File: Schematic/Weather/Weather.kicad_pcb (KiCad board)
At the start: 2 copper layers, 38 parts, among them J1 4_Way_Wire, J2 4_Way_Wire, J3 4_Way_Wire, Q1 BSS138, Q2 AO3401, Q3 AO3401, U1 AMS1117, U2 ESP-01v090, U3 AMS1117, U4 ESP-01v090, U5 LM321

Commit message: small compnent changes
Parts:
- moved R1 81.1 mm to (118.1, -120.7), turned to 90 degrees
- moved R2 77.2 mm to (113.0, -120.7), turned to 90 degrees
- moved C3 69.2 mm to (115.6, -116.8), turned to 270 degrees
- moved C2 68.6 mm to (106.7, -114.3), turned to 270 degrees
- moved C1 67.4 mm to (106.7, -128.3), turned to 180 degrees
- moved U2 64.4 mm to (94.0, -123.2), turned to 270 degrees
- moved PSU1 62.0 mm to (160.0, -125.7), turned to 270 degrees
- moved MOD2 60.0 mm to (123.2, -113.0), turned to 90 degrees
- moved J1 57.2 mm to (144.1, -170.0)
- moved U3 57.2 mm to (151.4, -168.2)
- moved U4 57.2 mm to (136.1, -167.9)
- moved U1 54.7 mm to (104.1, -120.7)
- moved R12 51.9 mm to (85.1, -181.6), turned to 270 degrees
- moved Q1 42.6 mm to (24.1, -167.6), turned to 90 degrees
- moved MOD1 41.9 mm to (123.2, -125.7), turned to 90 degrees
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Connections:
- MOD1 pad 2: Net-(MOD1-Pad2) -> GND
- MOD1 pad 3: GND -> /Internal ESP8266/J3_P3
- MOD1 pad 4: /Internal ESP8266/J3_P3 -> /Internal ESP8266/J3_P2
- MOD2 pad 1: /Internal ESP8266/J3_P3 -> /PSU 1/J1_P2
- MOD2 pad 2: /Internal ESP8266/J3_P2 -> GND
- MOD2 pad 3: /PSU 1/J1_P2 -> /Internal ESP8266/J3_P3
- MOD2 pad 4: GND -> /Internal ESP8266/J3_P2
- Q3 pad 2: Net-(Q3-Pad2) -> Vdrive
- R12 pad 1: Net-(R12-Pad1) -> Vdrive

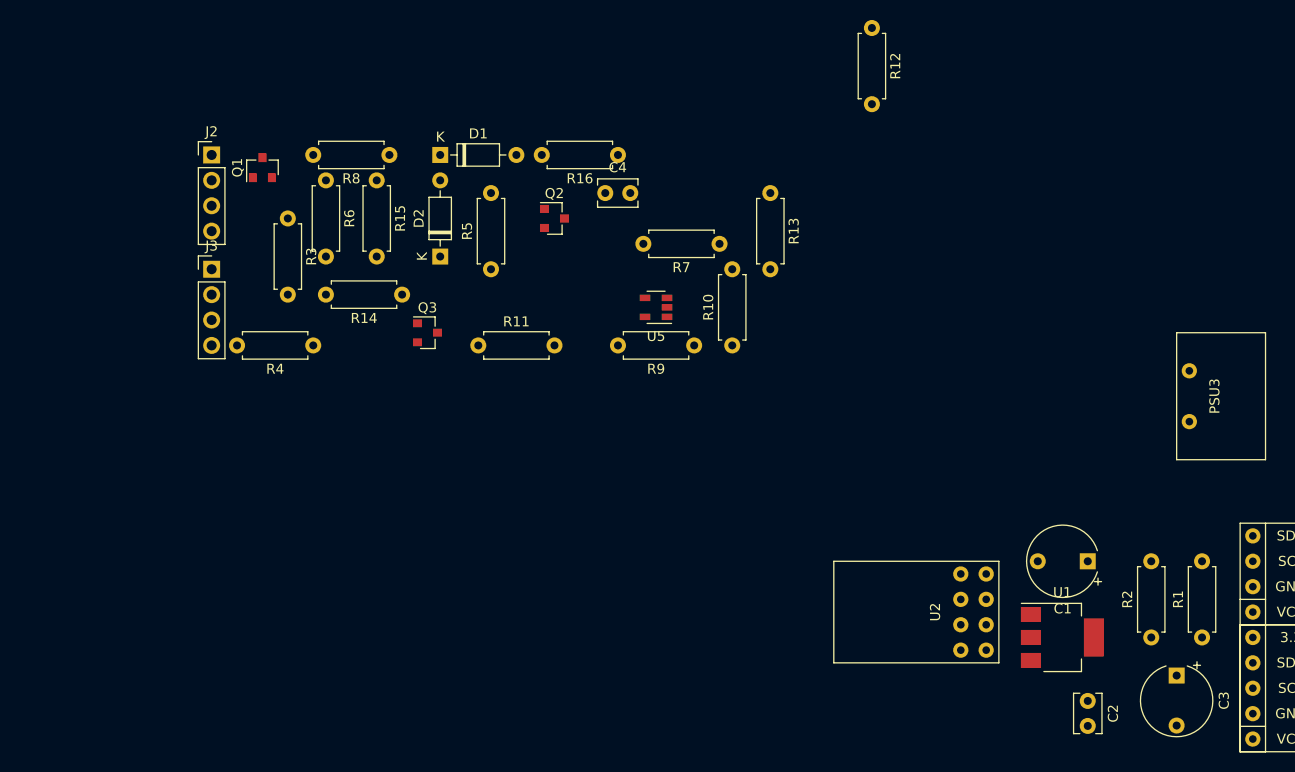
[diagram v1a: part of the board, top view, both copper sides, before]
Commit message: Borad layout 2x for Tx Rx
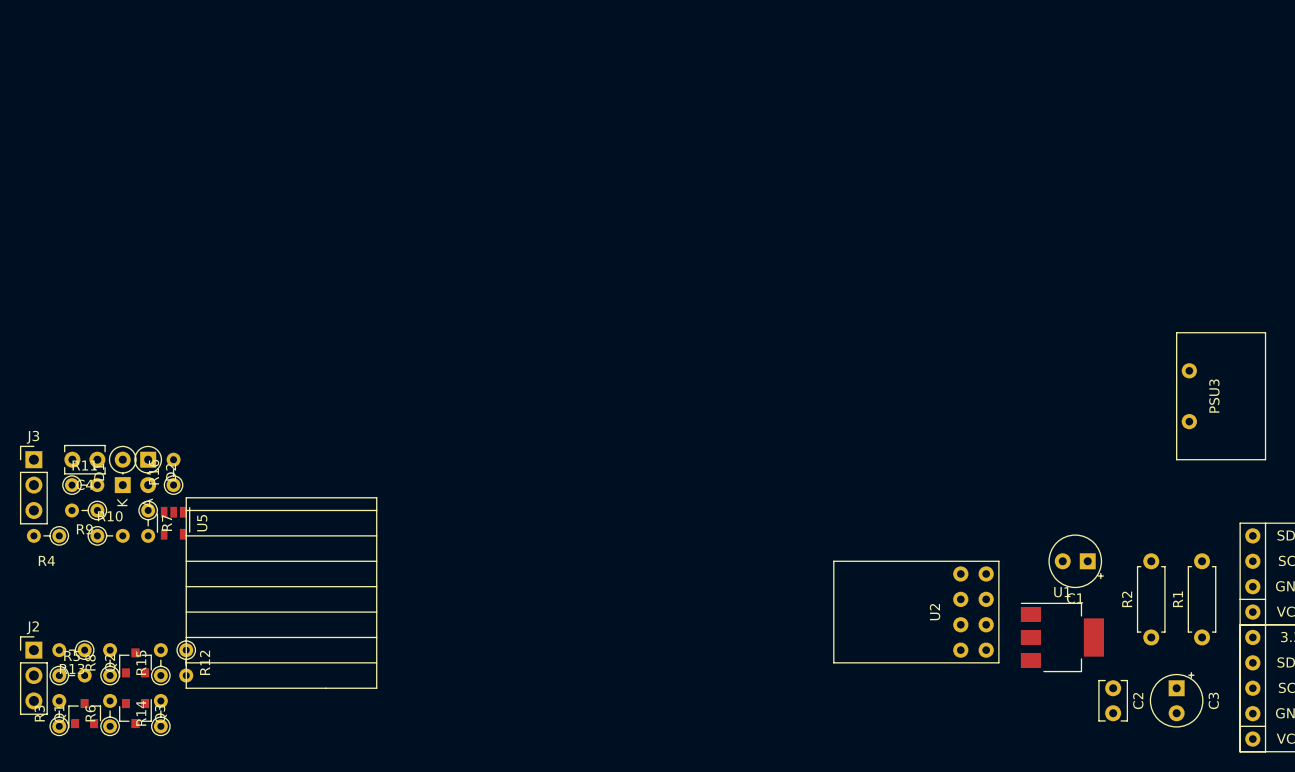
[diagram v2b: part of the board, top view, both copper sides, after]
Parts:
- C1, C3: footprint Capacitor_THT:CP_Radial_Tantal_D7.0mm_P5.00mm -> Capacitor_THT:CP_Radial_Tantal_D5.0mm_P2.50mm
- D1: footprint Diode_THT:D_DO-35_SOD27_P7.62mm_Horizontal -> Diode_THT:D_DO-35_SOD27_P2.54mm_Vertical_KathodeUp
- D2: footprint Diode_THT:D_DO-35_SOD27_P7.62mm_Horizontal -> Diode_THT:D_DO-35_SOD27_P2.54mm_Vertical_AnodeUp
- J2, J3: value 4_Way_Wire -> 3_Way_Wire; footprint Connector_PinHeader_2.54mm:PinHeader_1x04_P2.54mm_Vertical -> Connector_PinHeader_2.54mm:PinHeader_1x03_P2.54mm_Vertical
- R10, R11, R12, R13, R14, R15, R16, R3, R4, R5, R6, R7, R8, R9: footprint Resistor_THT:R_Axial_DIN0207_L6.3mm_D2.5mm_P7.62mm_Horizontal -> Resistor_THT:R_Axial_DIN0204_L3.6mm_D1.6mm_P2.54mm_Vertical
- moved R12 92.6 mm to (16.5, -119.4)
- moved R13 82.4 mm to (6.35, -119.4), turned to 180 degrees
- moved R10 66.3 mm to (7.62, -130.8), turned to 0 degrees
- moved R7 63.1 mm to (12.7, -133.3), turned to 270 degrees
- moved R9 61.9 mm to (7.62, -133.3)
- moved Q2 61.1 mm to (11.4, -118.1), turned to 90 degrees
- moved R5 59.3 mm to (3.81, -116.8), turned to 0 degrees
- moved R8 59.1 mm to (8.89, -116.8), turned to 90 degrees
- moved R6 58.7 mm to (8.89, -111.8), turned to 90 degrees
- moved Q1 57.4 mm to (6.35, -113.0)
- moved C4 57.4 mm to (7.62, -138.4), turned to 180 degrees
- moved R3 55.7 mm to (3.81, -111.8), turned to 90 degrees
- moved R16 55.4 mm to (15.2, -135.9), turned to 90 degrees
- moved R15 54.0 mm to (14.0, -116.8), turned to 90 degrees
- moved U5 52.9 mm to (15.2, -132.1), turned to 270 degrees
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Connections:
- J1 pad 1: Net-(J1-Pad1) -> (no net)
- J1 pad 2: Net-(J1-Pad2) -> (no net)
- J1 pad 3: Net-(J1-Pad3) -> (no net)
- J1 pad 4: Net-(J1-Pad4) -> (no net)
- J2 pad 2: /Anenometer Control Board/J13_P2 -> /Anenometer Control Board/J13_P4
- J2 pad 3: GNDS -> /Anenometer Control Board/J13_P5
- J3 pad 2: /Anenometer Control Board/J13_P6 -> /Anenometer Control Board/J13_P2
- J3 pad 3: GNDS -> /Anenometer Control Board/J13_P3
- PSU2 pad 2: /PSU 2/J5_P2 -> (no net)
- PSU3 pad 2: /PSU 2/J5_P3 -> (no net)
- R3 pad 2: /Anenometer Control Board/J13_P6 -> /Anenometer Control Board/J13_P5
- R4 pad 2: /Anenometer Control Board/J13_P8 -> /Anenometer Control Board/J13_P3
- U2 pad 1: Net-(U2-Pad1) -> (no net)
- U2 pad 8: Net-(U2-Pad8) -> (no net)
- U3 pad 3: Net-(U3-Pad3) -> (no net)
- U4 pad 1: Net-(U4-Pad1) -> (no net)
- U4 pad 3: Net-(U4-Pad3) -> (no net)
- U4 pad 4: Net-(U4-Pad4) -> (no net)
- U4 pad 5: Net-(U4-Pad5) -> (no net)
- U4 pad 6: Net-(U4-Pad6) -> (no net)
- U4 pad 8: Net-(U4-Pad8) -> (no net)

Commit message: board rework
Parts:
- moved R7 2.54 mm to (12.7, -130.8), turned to 90 degrees
- moved U5 1.27 mm to (16.5, -132.1), turned to 0 degrees
- moved J3 1.27 mm to (2.54, -138.4)
- moved R4 1.27 mm to (5.08, -130.8)
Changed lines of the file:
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@@
     (solder_mask_min_width 0.25)
     (aux_axis_origin 0 0)
-    (visible_elements 7FFFEFFF)
+    (visible_elements 7FFFFFFF)
     (pcbplotparams
       (layerselection 0x010fc_ffffffff)
@@
   )
   (module Connector_PinHeader_2.54mm:PinHeader_1x03_P2.54mm_Vertical (layer F.Cu)
-    (at 1.27 -138.43)
+    (at 2.54 -138.43)
     (descr "Through hole straight pin header, 1x03, 2.54mm pitch, single row")
     (tags "Through hole pin header THT 1x03 2.54mm single row")
@@
   )
   (module Resistor_THT:R_Axial_DIN0204_L3.6mm_D1.6mm_P2.54mm_Vertical (layer F.Cu)
-    (at 12.7 -133.35 270)
-    (descr "Resistor, Axial_DIN0204 series, Axial, Vertical, pin pitch=2.54mm, 0.167W, length*diameter=3.6*1.6mm^2, http://cdn-reichelt.de/documents/datenblatt/B400/1_4W%23YAG.pdf")
-    (tags "Resistor Axial_DIN0204 series Axial Vertical pin pitch 2.54mm 0.167W length 3.6mm diameter 1.6mm")
-    (fp_text reference R7 (at 1.27 -1.92 270) (layer F.SilkS)
-      (effects (font (size 1 1) (thickness 0.15)))
-    )
-    (fp_text value 4.7K (at 1.27 1.92 270) (layer F.Fab)
-      (effects (font (size 1 1) (thickness 0.15)))
-    )
-    (fp_text user %R (at 1.27 -1.92 270) (layer F.Fab)
-      (effects (font (size 1 1) (thickness 0.15)))
-    )
-    (fp_line (start 3.49 -1.05) (end -1.05 -1.05) (layer F.CrtYd) (width 0.05))
-    (fp_line (start 3.49 1.05) (end 3.49 -1.05) (layer F.CrtYd) (width 0.05))
-    (fp_line (start -1.05 1.05) (end 3.49 1.05) (layer F.CrtYd) (width 0.05))
-    (fp_line (start -1.05 -1.05) (end -1.05 1.05) (layer F.CrtYd) (width 0.05))
-    (fp_line (start 0.92 0) (end 1.54 0) (layer F.SilkS) (width 0.12))
-    (fp_line (start 0 0) (end 2.54 0) (layer F.Fab) (width 0.1))
-    (fp_circle (center 0 0) (end 0.92 0) (layer F.SilkS) (width 0.12))
-    (fp_circle (center 0 0) (end 0.8 0) (layer F.Fab) (width 0.1))
-    (pad 2 thru_hole oval (at 2.54 0 270) (size 1.4 1.4) (drill 0.7) (layers *.Cu *.Mask)
+    (at 12.7 -130.81 90)
+    (descr "Resistor, Axial_DIN0204 series, Axial, Vertical, pin pitch=2.54mm, 0.167W, length*diameter=3.6*1.6mm^2, http://cdn-reichelt.de/documents/datenblatt/B400/1_4W%23YAG.pdf")
+    (tags "Resistor Axial_DIN0204 series Axial Vertical pin pitch 2.54mm 0.167W length 3.6mm diameter 1.6mm")
+    (fp_text reference R7 (at 1.27 -1.92 90) (layer F.SilkS)
+      (effects (font (size 1 1) (thickness 0.15)))
+    )
+    (fp_text value 4.7K (at 1.27 1.92 90) (layer F.Fab)
+      (effects (font (size 1 1) (thickness 0.15)))
+    )
+    (fp_text user %R (at 1.27 -1.92 90) (layer F.Fab)
+      (effects (font (size 1 1) (thickness 0.15)))
+    )
+    (fp_line (start 3.49 -1.05) (end -1.05 -1.05) (layer F.CrtYd) (width 0.05))
+    (fp_line (start 3.49 1.05) (end 3.49 -1.05) (layer F.CrtYd) (width 0.05))
+    (fp_line (start -1.05 1.05) (end 3.49 1.05) (layer F.CrtYd) (width 0.05))
+    (fp_line (start -1.05 -1.05) (end -1.05 1.05) (layer F.CrtYd) (width 0.05))
+    (fp_line (start 0.92 0) (end 1.54 0) (layer F.SilkS) (width 0.12))
+    (fp_line (start 0 0) (end 2.54 0) (layer F.Fab) (width 0.1))
+    (fp_circle (center 0 0) (end 0.92 0) (layer F.SilkS) (width 0.12))
+    (fp_circle (center 0 0) (end 0.8 0) (layer F.Fab) (width 0.1))
+    (pad 2 thru_hole oval (at 2.54 0 90) (size 1.4 1.4) (drill 0.7) (layers *.Cu *.Mask)
       (net 20 "Net-(R4-Pad1)"))
-    (pad 1 thru_hole circle (at 0 0 270) (size 1.4 1.4) (drill 0.7) (layers *.Cu *.Mask)
+    (pad 1 thru_hole circle (at 0 0 90) (size 1.4 1.4) (drill 0.7) (layers *.Cu *.Mask)
       (net 21 "Net-(R11-Pad2)"))
     (model ${KISYS3DMOD}/Resistor_THT.3dshapes/R_Axial_DIN0204_L3.6mm_D1.6mm_P2.54mm_Vertical.wrl
@@
   )
   (module Resistor_THT:R_Axial_DIN0204_L3.6mm_D1.6mm_P2.54mm_Vertical (layer F.Cu)
-    (at 3.81 -130.81 180)
+    (at 5.08 -130.81 180)
     (descr "Resistor, Axial_DIN0204 series, Axial, Vertical, pin pitch=2.54mm, 0.167W, length*diameter=3.6*1.6mm^2, http://cdn-reichelt.de/documents/datenblatt/B400/1_4W%23YAG.pdf")
     (tags "Resistor Axial_DIN0204 series Axial Vertical pin pitch 2.54mm 0.167W length 3.6mm diameter 1.6mm")
@@
   )
   (module Package_TO_SOT_SMD:SOT-23-5 (layer F.Cu)
-    (at 15.24 -132.08 270)
+    (at 16.51 -132.08)
     (descr "5-pin SOT23 package")
     (tags SOT-23-5)
     (attr smd)
-    (fp_text reference U5 (at 0 -2.9 270) (layer F.SilkS)
-      (effects (font (size 1 1) (thickness 0.15)))
-    )
-    (fp_text value LM321 (at 0 2.9 270) (layer F.Fab)
+    (fp_text reference U5 (at 0 -2.9) (layer F.SilkS)
+      (effects (font (size 1 1) (thickness 0.15)))
+    )
+    (fp_text value LM321 (at 0 2.9) (layer F.Fab)
       (effects (font (size 1 1) (thickness 0.15)))
     )
@@
     (fp_line (start 0.9 -1.61) (end -1.55 -1.61) (layer F.SilkS) (width 0.12))
     (fp_line (start -0.9 1.61) (end 0.9 1.61) (layer F.SilkS) (width 0.12))
-    (fp_text user %R (at 0 0) (layer F.Fab)
+    (fp_text user %R (at 0 0 -270) (layer F.Fab)
       (effects (font (size 0.5 0.5) (thickness 0.075)))
     )
-    (pad 5 smd rect (at 1.1 -0.95 270) (size 1.06 0.65) (layers F.Cu F.Paste F.Mask)
+    (pad 5 smd rect (at 1.1 -0.95) (size 1.06 0.65) (layers F.Cu F.Paste F.Mask)
       (net 8 "/Anenometer Control Board/J13_P2"))
-    (pad 4 smd rect (at 1.1 0.95 270) (size 1.06 0.65) (layers F.Cu F.Paste F.Mask)
+    (pad 4 smd rect (at 1.1 0.95) (size 1.06 0.65) (layers F.Cu F.Paste F.Mask)
       (net 20 "Net-(R4-Pad1)"))
-    (pad 3 smd rect (at -1.1 0.95 270) (size 1.06 0.65) (layers F.Cu F.Paste F.Mask)
+    (pad 3 smd rect (at -1.1 0.95) (size 1.06 0.65) (layers F.Cu F.Paste F.Mask)
       (net 21 "Net-(R11-Pad2)"))
-    (pad 2 smd rect (at -1.1 0 270) (size 1.06 0.65) (layers F.Cu F.Paste F.Mask)
-      (net 6 GNDS))
-    (pad 1 smd rect (at -1.1 -0.95 270) (size 1.06 0.65) (layers F.Cu F.Paste F.Mask)
+    (pad 2 smd rect (at -1.1 0) (size 1.06 0.65) (layers F.Cu F.Paste F.Mask)
+      (net 6 GNDS))
+    (pad 1 smd rect (at -1.1 -0.95) (size 1.06 0.65) (layers F.Cu F.Paste F.Mask)
       (net 22 "Net-(R10-Pad1)"))
     (model ${KISYS3DMOD}/Package_TO_SOT_SMD.3dshapes/SOT-23-5.wrl

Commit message: update before south board added
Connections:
- J1 pad 1: (no net) -> Net-(J1-Pad1)
- J1 pad 2: (no net) -> Net-(J1-Pad2)
- J1 pad 3: (no net) -> Net-(J1-Pad3)
- J1 pad 4: (no net) -> Net-(J1-Pad4)
- PSU2 pad 2: (no net) -> /PSU 2/J5_P2
- PSU3 pad 2: (no net) -> /PSU 2/J5_P3
- U2 pad 1: (no net) -> Net-(U2-Pad1)
- U2 pad 8: (no net) -> Net-(U2-Pad8)
- U3 pad 3: (no net) -> Net-(U3-Pad3)
- U4 pad 1: (no net) -> Net-(U4-Pad1)
- U4 pad 3: (no net) -> Net-(U4-Pad3)
- U4 pad 4: (no net) -> Net-(U4-Pad4)
- U4 pad 5: (no net) -> Net-(U4-Pad5)
- U4 pad 6: (no net) -> Net-(U4-Pad6)
- U4 pad 8: (no net) -> Net-(U4-Pad8)
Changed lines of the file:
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@@
     (zones 0)
     (modules 38)
-    (nets 27)
+    (nets 42)
   )
   (page A4)
@@
     (solder_mask_min_width 0.25)
     (aux_axis_origin 0 0)
-    (visible_elements 7FFFFFFF)
+    (visible_elements 7FFFEFFF)
     (pcbplotparams
       (layerselection 0x010fc_ffffffff)
@@
   (net 25 "/Anenometer Control Board/J13_P5")
   (net 26 "/Anenometer Control Board/J13_P3")
+  (net 27 "Net-(J1-Pad4)")
+  (net 28 "Net-(J1-Pad3)")
+  (net 29 "Net-(J1-Pad2)")
+  (net 30 "Net-(J1-Pad1)")
+  (net 31 "/PSU 2/J5_P2")
+  (net 32 "/PSU 2/J5_P3")
+  (net 33 "Net-(U2-Pad8)")
+  (net 34 "Net-(U2-Pad1)")
+  (net 35 "Net-(U3-Pad3)")
+  (net 36 "Net-(U4-Pad8)")
+  (net 37 "Net-(U4-Pad6)")
+  (net 38 "Net-(U4-Pad5)")
+  (net 39 "Net-(U4-Pad4)")
+  (net 40 "Net-(U4-Pad3)")
+  (net 41 "Net-(U4-Pad1)")
   (net_class Default "This is the default net class."
     (clearance 0.2)
@@
     (add_net "/PSU 1/J1_P2")
     (add_net "/PSU 2/J5_P1")
+    (add_net "/PSU 2/J5_P2")
+    (add_net "/PSU 2/J5_P3")
     (add_net GND)
     (add_net GNDS)
@@
     (add_net "Net-(C4-Pad1)")
     (add_net "Net-(C4-Pad2)")
+    (add_net "Net-(J1-Pad1)")
+    (add_net "Net-(J1-Pad2)")
+    (add_net "Net-(J1-Pad3)")
+    (add_net "Net-(J1-Pad4)")
     (add_net "Net-(Q1-Pad1)")
     (add_net "Net-(Q1-Pad3)")
@@
     (add_net "Net-(R2-Pad2)")
     (add_net "Net-(R4-Pad1)")
+    (add_net "Net-(U2-Pad1)")
+    (add_net "Net-(U2-Pad8)")
     (add_net "Net-(U3-Pad1)")
     (add_net "Net-(U3-Pad2)")
+    (add_net "Net-(U3-Pad3)")
+    (add_net "Net-(U4-Pad1)")
+    (add_net "Net-(U4-Pad3)")
+    (add_net "Net-(U4-Pad4)")
+    (add_net "Net-(U4-Pad5)")
+    (add_net "Net-(U4-Pad6)")
+    (add_net "Net-(U4-Pad8)")
     (add_net Vdrive)
   )
@@
     (fp_line (start 5.08 -3.81) (end 5.08 12.7) (layer F.SilkS) (width 0.12))
     (fp_line (start -5.08 -3.81) (end 5.08 -3.81) (layer F.SilkS) (width 0.12))
-    (pad 8 thru_hole circle (at 3.81 0) (size 1.524 1.524) (drill 0.762) (layers *.Cu *.Mask))
+    (pad 8 thru_hole circle (at 3.81 0) (size 1.524 1.524) (drill 0.762) (layers *.Cu *.Mask)
+      (net 36 "Net-(U4-Pad8)"))
     (pad 7 thru_hole circle (at 1.27 0) (size 1.524 1.524) (drill 0.762) (layers *.Cu *.Mask)
       (net 24 "Net-(U3-Pad2)"))
-    (pad 6 thru_hole circle (at -1.27 0) (size 1.524 1.524) (drill 0.762) (layers *.Cu *.Mask))
-    (pad 5 thru_hole circle (at -3.81 0) (size 1.524 1.524) (drill 0.762) (layers *.Cu *.Mask))
-    (pad 4 thru_hole circle (at 3.81 -2.54) (size 1.524 1.524) (drill 0.762) (layers *.Cu *.Mask))
-    (pad 3 thru_hole circle (at 1.27 -2.54) (size 1.524 1.524) (drill 0.762) (layers *.Cu *.Mask))
+    (pad 6 thru_hole circle (at -1.27 0) (size 1.524 1.524) (drill 0.762) (layers *.Cu *.Mask)
+      (net 37 "Net-(U4-Pad6)"))
+    (pad 5 thru_hole circle (at -3.81 0) (size 1.524 1.524) (drill 0.762) (layers *.Cu *.Mask)
+      (net 38 "Net-(U4-Pad5)"))
+    (pad 4 thru_hole circle (at 3.81 -2.54) (size 1.524 1.524) (drill 0.762) (layers *.Cu *.Mask)
+      (net 39 "Net-(U4-Pad4)"))
+    (pad 3 thru_hole circle (at 1.27 -2.54) (size 1.524 1.524) (drill 0.762) (layers *.Cu *.Mask)
+      (net 40 "Net-(U4-Pad3)"))
     (pad 2 thru_hole circle (at -1.27 -2.54) (size 1.524 1.524) (drill 0.762) (layers *.Cu *.Mask)
       (net 23 "Net-(U3-Pad1)"))
-    (pad 1 thru_hole circle (at -3.81 -2.54) (size 1.524 1.524) (drill 0.762) (layers *.Cu *.Mask))
+    (pad 1 thru_hole circle (at -3.81 -2.54) (size 1.524 1.524) (drill 0.762) (layers *.Cu *.Mask)
+      (net 41 "Net-(U4-Pad1)"))
   )
   (module Package_TO_SOT_SMD:SOT-223-3_TabPin2 (layer F.Cu)
@@
     (pad 1 smd rect (at -3.15 -2.3) (size 2 1.5) (layers F.Cu F.Paste F.Mask)
       (net 23 "Net-(U3-Pad1)"))
-    (pad 3 smd rect (at -3.15 2.3) (size 2 1.5) (layers F.Cu F.Paste F.Mask))
+    (pad 3 smd rect (at -3.15 2.3) (size 2 1.5) (layers F.Cu F.Paste F.Mask)
+      (net 35 "Net-(U3-Pad3)"))
     (pad 2 smd rect (at -3.15 0) (size 2 1.5) (layers F.Cu F.Paste F.Mask)
       (net 24 "Net-(U3-Pad2)"))
@@
     (fp_line (start 5.08 -3.81) (end 5.08 12.7) (layer F.SilkS) (width 0.12))
     (fp_line (start -5.08 -3.81) (end 5.08 -3.81) (layer F.SilkS) (width 0.12))
-    (pad 8 thru_hole circle (at 3.81 0 270) (size 1.524 1.524) (drill 0.762) (layers *.Cu *.Mask))
+    (pad 8 thru_hole circle (at 3.81 0 270) (size 1.524 1.524) (drill 0.762) (layers *.Cu *.Mask)
+      (net 33 "Net-(U2-Pad8)"))
     (pad 7 thru_hole circle (at 1.27 0 270) (size 1.524 1.524) (drill 0.762) (layers *.Cu *.Mask)
       (net 3 "Net-(C2-Pad1)"))
@@
     (pad 2 thru_hole circle (at -1.27 -2.54 270) (size 1.524 1.524) (drill 0.762) (layers *.Cu *.Mask)
       (net 1 GND))
-    (pad 1 thru_hole circle (at -3.81 -2.54 270) (size 1.524 1.524) (drill 0.762) (layers *.Cu *.Mask))
+    (pad 1 thru_hole circle (at -3.81 -2.54 270) (size 1.524 1.524) (drill 0.762) (layers *.Cu *.Mask)
+      (net 34 "Net-(U2-Pad1)"))
   )
   (module Package_TO_SOT_SMD:SOT-223-3_TabPin2 (layer F.Cu)
@@
     (fp_line (start 6.35 -2.54) (end 6.35 6.35) (layer F.SilkS) (width 0.12))
     (fp_line (start -6.35 -2.54) (end 6.35 -2.54) (layer F.SilkS) (width 0.12))
-    (pad 2 thru_hole circle (at 2.54 -1.27 90) (size 1.524 1.524) (drill 0.762) (layers *.Cu *.Mask))
+    (pad 2 thru_hole circle (at 2.54 -1.27 90) (size 1.524 1.524) (drill 0.762) (layers *.Cu *.Mask)
+      (net 32 "/PSU 2/J5_P3"))
     (pad 1 thru_hole circle (at -2.54 -1.27 90) (size 1.524 1.524) (drill 0.762) (layers *.Cu *.Mask)
       (net 11 "/PSU 2/J5_P1"))
@@
     (fp_line (start 6.35 -2.54) (end 6.35 6.35) (layer F.SilkS) (width 0.12))
     (fp_line (start -6.35 -2.54) (end 6.35 -2.54) (layer F.SilkS) (width 0.12))
-    (pad 2 thru_hole circle (at 2.54 -1.27 90) (size 1.524 1.524) (drill 0.762) (layers *.Cu *.Mask))
+    (pad 2 thru_hole circle (at 2.54 -1.27 90) (size 1.524 1.524) (drill 0.762) (layers *.Cu *.Mask)
+      (net 31 "/PSU 2/J5_P2"))
     (pad 1 thru_hole circle (at -2.54 -1.27 90) (size 1.524 1.524) (drill 0.762) (layers *.Cu *.Mask)
       (net 11 "/PSU 2/J5_P1"))
@@
     (fp_line (start 1.27 -1.27) (end 1.27 8.89) (layer F.Fab) (width 0.1))
     (fp_line (start -0.635 -1.27) (end 1.27 -1.27) (layer F.Fab) (width 0.1))
-    (pad 4 thru_hole oval (at 0 7.62) (size 1.7 1.7) (drill 1) (layers *.Cu *.Mask))
-    (pad 3 thru_hole oval (at 0 5.08) (size 1.7 1.7) (drill 1) (layers *.Cu *.Mask))
-    (pad 2 thru_hole oval (at 0 2.54) (size 1.7 1.7) (drill 1) (layers *.Cu *.Mask))
-    (pad 1 thru_hole rect (at 0 0) (size 1.7 1.7) (drill 1) (layers *.Cu *.Mask))
+    (pad 4 thru_hole oval (at 0 7.62) (size 1.7 1.7) (drill 1) (layers *.Cu *.Mask)
+      (net 27 "Net-(J1-Pad4)"))
+    (pad 3 thru_hole oval (at 0 5.08) (size 1.7 1.7) (drill 1) (layers *.Cu *.Mask)
+      (net 28 "Net-(J1-Pad3)"))
+    (pad 2 thru_hole oval (at 0 2.54) (size 1.7 1.7) (drill 1) (layers *.Cu *.Mask)
+      (net 29 "Net-(J1-Pad2)"))
+    (pad 1 thru_hole rect (at 0 0) (size 1.7 1.7) (drill 1) (layers *.Cu *.Mask)
+      (net 30 "Net-(J1-Pad1)"))
     (model ${KISYS3DMOD}/Connector_PinHeader_2.54mm.3dshapes/PinHeader_1x04_P2.54mm_Vertical.wrl
       (at (xyz 0 0 0))
